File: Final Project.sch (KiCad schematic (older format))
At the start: 22 parts, among them Q1 2N7000, Q5 BS250, Q7 2N7000

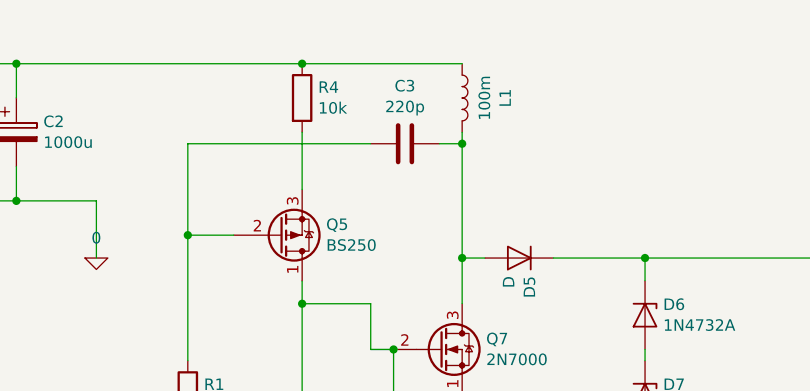
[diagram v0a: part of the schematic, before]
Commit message: Changed Capacitor
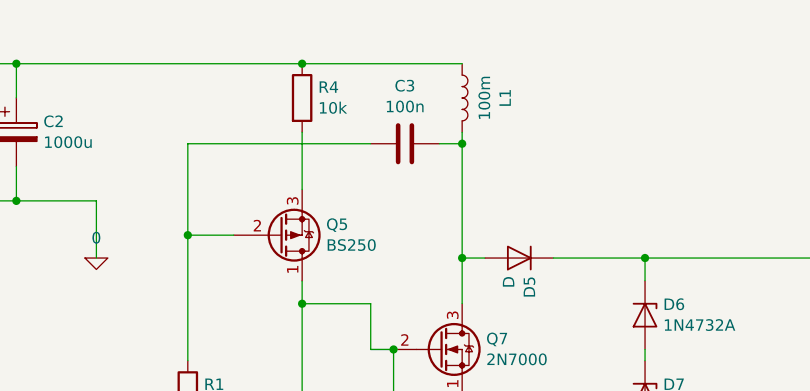
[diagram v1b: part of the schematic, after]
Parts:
- C3: value 220p -> 100n; Spice_Model 220p -> 100n
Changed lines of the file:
@@
 P 5050 1250
 F 0 "C3" V 4798 1250 50  0000 C CNN
-F 1 "220p" V 4889 1250 50  0000 C CNN
+F 1 "100n" V 4889 1250 50  0000 C CNN
 F 2 "" H 5088 1100 50  0001 C CNN
 F 3 "~" H 5050 1250 50  0001 C CNN
 F 4 "C" H 5050 1250 50  0001 C CNN "Spice_Primitive"
-F 5 "220p" H 5050 1250 50  0001 C CNN "Spice_Model"
+F 5 "100n" H 5050 1250 50  0001 C CNN "Spice_Model"
 F 6 "Y" H 5050 1250 50  0001 C CNN "Spice_Netlist_Enabled"
 	1    5050 1250
